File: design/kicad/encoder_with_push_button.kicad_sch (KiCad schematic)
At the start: 1 part

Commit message: Refactor code structure for improved readability and maintainability
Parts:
- added D4, D5, D6: PESD5V0L1BA,115, KiCad:SOD2512X110N, symbol PESD5V0L1BA_115:PESD5V0L1BA,115
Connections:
- net QUAD_A: now also D4.1 (K1)
- net QUAD_B: now also D5.1 (K1)
- net SW_A: now also D6.1 (K1)
- new net GND: D4.2 (K2), D5.2 (K2), D6.2 (K2)

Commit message: Add schematic for MIDI Display MSP2807 with associated components
- Created a new schematic file for the MIDI Display MSP2807.
- Included a unpolarized capacitor (C2) with a value of 100nF.
- Added properties such as reference, value, footprint, and datasheet for the capacitor.
- Integrated the MIDI Display module with detailed pin configurations and properties.
- Defined hierarchical labels for power and data connections (VCC, GND, CS, RST, DC, etc.).
- Ensured all components are marked for BOM inclusion and simulation.
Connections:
- net QUAD_GND is gone; now on net GND: ENC_MECH1.C (GND)
- net SW_GND is gone; now on net GND: ENC_MECH1.2 (GND)
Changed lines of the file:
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@@
-	(wire
-		(pts
-			(xy 50.8 76.2) (xy 87.63 76.2)
-		)
-		(stroke
-			(width 0)
-			(type default)
-		)
-	)
-	(wire
-		(pts
-			(xy 115.57 78.74) (xy 118.11 78.74)
-		)
-		(stroke
-			(width 0)
-			(type default)
-		)
-	)
 	(wire
 		(pts
@@
 	(wire
 		(pts
+			(xy 115.57 78.74) (xy 116.84 78.74)
+		)
+		(stroke
+			(width 0)
+			(type default)
+		)
+	)
+	(wire
+		(pts
 			(xy 50.8 91.44) (xy 63.5 91.44)
 		)
@@
 	(wire
 		(pts
+			(xy 86.36 76.2) (xy 87.63 76.2)
+		)
+		(stroke
+			(width 0)
+			(type default)
+		)
+	)
+	(wire
+		(pts
 			(xy 86.36 78.74) (xy 87.63 78.74)
 		)
@@
 			(width 0)
 			(type default)
+		)
+	)
+	(global_label "GND"
+		(shape input)
+		(at 116.84 78.74 0)
+		(fields_autoplaced yes)
+		(effects
+			(font
+				(size 1.27 1.27)
+			)
+			(justify left)
+		)
+		(property "Intersheetrefs" "${INTERSHEET_REFS}"
+			(at 123.6957 78.74 0)
+			(effects
+				(font
+					(size 1.27 1.27)
+				)
+				(justify left)
+				(hide yes)
+			)
+		)
+	)
+	(global_label "GND"
+		(shape input)
+		(at 86.36 76.2 180)
+		(fields_autoplaced yes)
+		(effects
+			(font
+				(size 1.27 1.27)
+			)
+			(justify right)
+		)
+		(property "Intersheetrefs" "${INTERSHEET_REFS}"
+			(at 79.5043 76.2 0)
+			(effects
+				(font
+					(size 1.27 1.27)
+				)
+				(justify right)
+				(hide yes)
+			)
 		)
 	)
@@
 		)
 	)
-	(hierarchical_label "QUAD_GND"
-		(shape passive)
-		(at 50.8 76.2 180)
-		(effects
-			(font
-				(size 1.27 1.27)
-			)
-			(justify right)
-		)
-	)
-	(hierarchical_label "SW_GND"
-		(shape passive)
-		(at 118.11 78.74 0)
-		(effects
-			(font
-				(size 1.27 1.27)
-			)
-			(justify left)
-		)
-	)

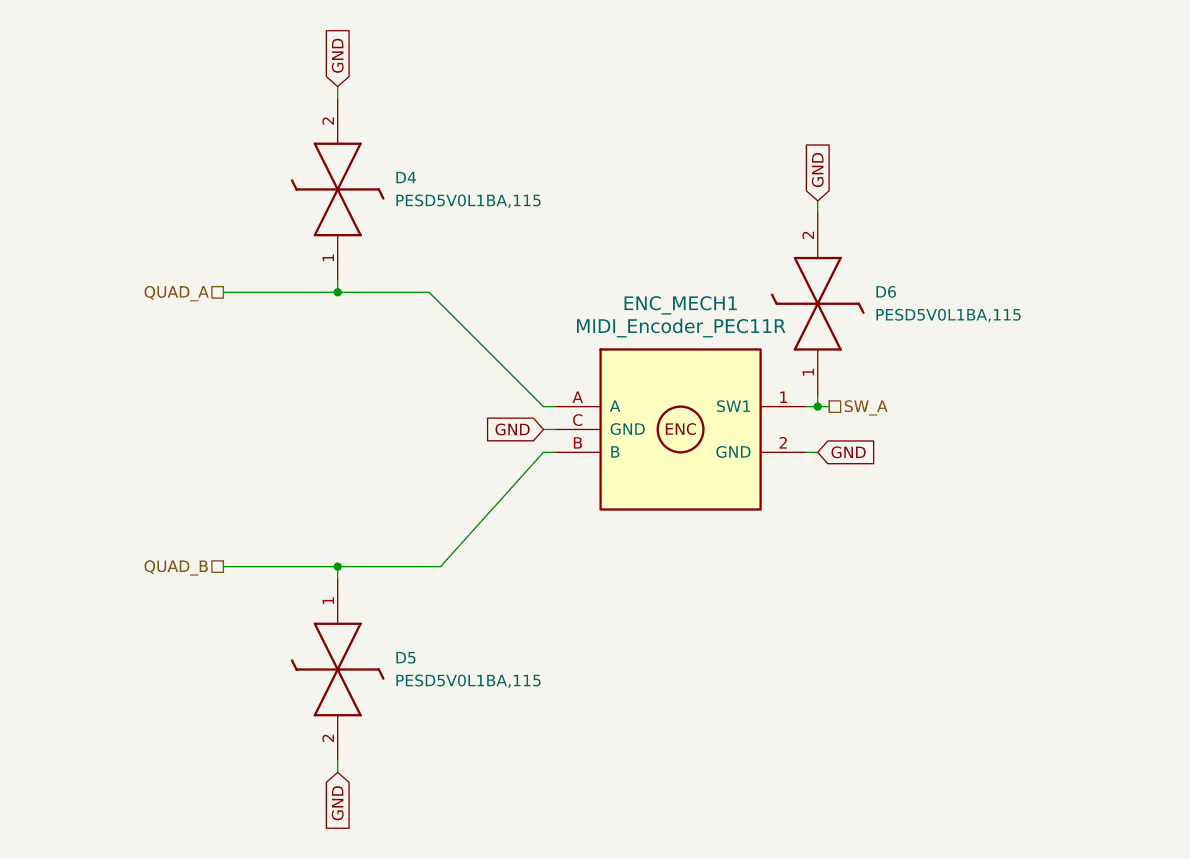
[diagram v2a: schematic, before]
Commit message: Fix net format name and update junctions in MIDI controller schematic
- Set net format name to "KiCad" in the project file.
- Added multiple junctions at specified coordinates in the schematic.
- Adjusted existing junction positions and UUIDs for consistency.
- Updated wire connections to reflect new junction placements.
- Corrected component references and properties for various components.
- Added new capacitor symbols with appropriate properties and references.
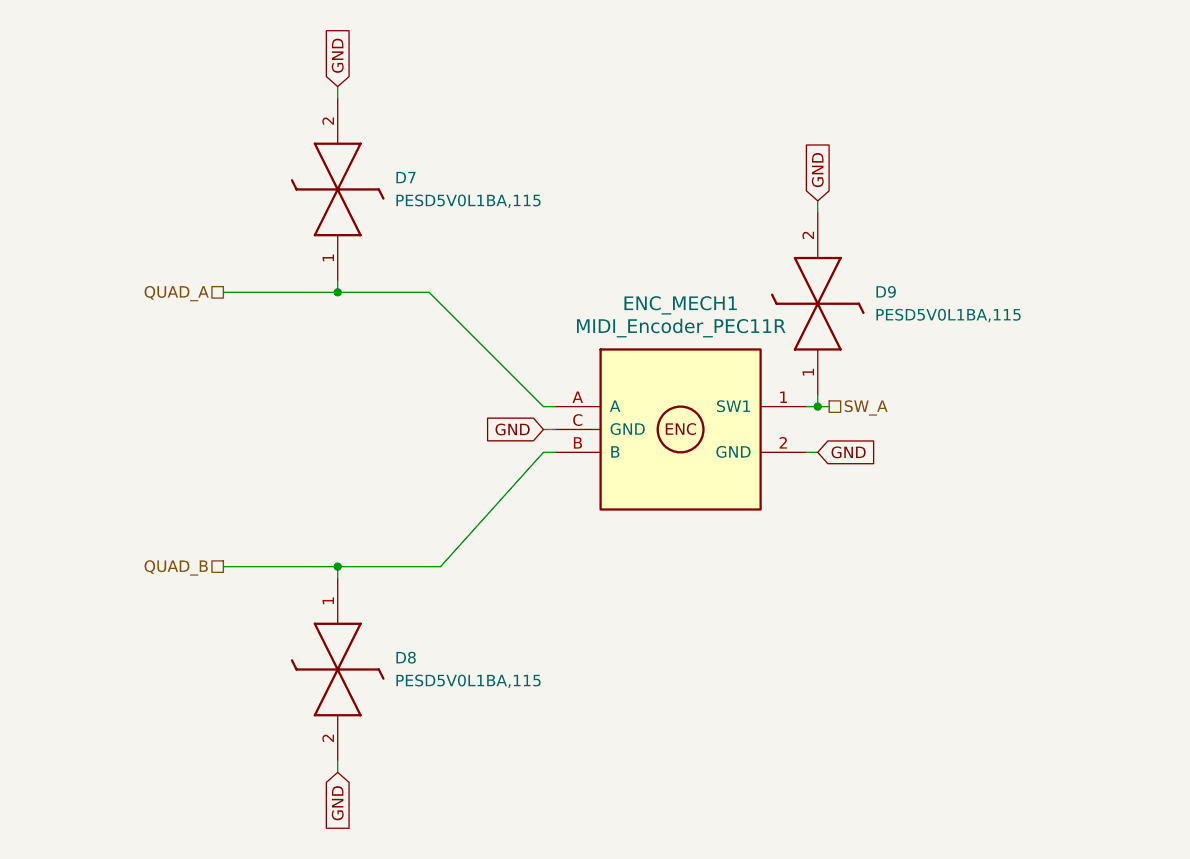
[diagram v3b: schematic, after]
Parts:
- renumbered D4 to D7, D5 to D8, D6 to D9
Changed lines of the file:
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@@
 		(dnp no)
 		(fields_autoplaced yes)
-		(property "Reference" "D4"
+		(property "Reference" "D7"
 			(at 69.85 48.2599 90)
 			(effects
@@
 			(project "midi_controller"
 				(path "/9e44e663-00d0-4f33-bf1f-c4ad78deb554/f2987add-55a5-4c89-9b33-db7ed86a6cdc"
+					(reference "D31")
+					(unit 1)
+				)
+				(path "/9e44e663-00d0-4f33-bf1f-c4ad78deb554/8b3bc88b-b526-44d8-9760-500b43fd5a71/0ace1318-b253-4d85-b784-aa61ad0f89cd"
+					(reference "D10")
+					(unit 1)
+				)
+				(path "/9e44e663-00d0-4f33-bf1f-c4ad78deb554/8b3bc88b-b526-44d8-9760-500b43fd5a71/1413c73c-0ad0-4a10-833c-ff3e4825f086"
+					(reference "D22")
+					(unit 1)
+				)
+				(path "/9e44e663-00d0-4f33-bf1f-c4ad78deb554/8b3bc88b-b526-44d8-9760-500b43fd5a71/24f763b3-d9d2-44ca-b0de-e5bd6d783cf4"
+					(reference "D25")
+					(unit 1)
+				)
+				(path "/9e44e663-00d0-4f33-bf1f-c4ad78deb554/8b3bc88b-b526-44d8-9760-500b43fd5a71/291f4e39-6718-4dda-83a6-20f8f943b75d"
+					(reference "D13")
+					(unit 1)
+				)
+				(path "/9e44e663-00d0-4f33-bf1f-c4ad78deb554/8b3bc88b-b526-44d8-9760-500b43fd5a71/3c9339b8-42f1-40cb-9183-aa88346af463"
+					(reference "D16")
+					(unit 1)
+				)
+				(path "/9e44e663-00d0-4f33-bf1f-c4ad78deb554/8b3bc88b-b526-44d8-9760-500b43fd5a71/4af660a9-1b0e-40bf-ba48-b976c7e464d4"
+					(reference "D19")
+					(unit 1)
+				)
+				(path "/9e44e663-00d0-4f33-bf1f-c4ad78deb554/8b3bc88b-b526-44d8-9760-500b43fd5a71/60e25267-b738-456c-86e0-26223ee5fe23"
+					(reference "D7")
+					(unit 1)
+				)
+				(path "/9e44e663-00d0-4f33-bf1f-c4ad78deb554/8b3bc88b-b526-44d8-9760-500b43fd5a71/761c51eb-8364-4d00-98cb-27a8734a6aa5"
 					(reference "D28")
-					(unit 1)
-				)
-				(path "/9e44e663-00d0-4f33-bf1f-c4ad78deb554/8b3bc88b-b526-44d8-9760-500b43fd5a71/0ace1318-b253-4d85-b784-aa61ad0f89cd"
-					(reference "D7")
-					(unit 1)
-				)
-				(path "/9e44e663-00d0-4f33-bf1f-c4ad78deb554/8b3bc88b-b526-44d8-9760-500b43fd5a71/1413c73c-0ad0-4a10-833c-ff3e4825f086"
-					(reference "D19")
-					(unit 1)
-				)
-				(path "/9e44e663-00d0-4f33-bf1f-c4ad78deb554/8b3bc88b-b526-44d8-9760-500b43fd5a71/24f763b3-d9d2-44ca-b0de-e5bd6d783cf4"
-					(reference "D22")
-					(unit 1)
-				)
-				(path "/9e44e663-00d0-4f33-bf1f-c4ad78deb554/8b3bc88b-b526-44d8-9760-500b43fd5a71/291f4e39-6718-4dda-83a6-20f8f943b75d"
-					(reference "D10")
-					(unit 1)
-				)
-				(path "/9e44e663-00d0-4f33-bf1f-c4ad78deb554/8b3bc88b-b526-44d8-9760-500b43fd5a71/3c9339b8-42f1-40cb-9183-aa88346af463"
-					(reference "D13")
-					(unit 1)
-				)
-				(path "/9e44e663-00d0-4f33-bf1f-c4ad78deb554/8b3bc88b-b526-44d8-9760-500b43fd5a71/4af660a9-1b0e-40bf-ba48-b976c7e464d4"
-					(reference "D16")
-					(unit 1)
-				)
-				(path "/9e44e663-00d0-4f33-bf1f-c4ad78deb554/8b3bc88b-b526-44d8-9760-500b43fd5a71/60e25267-b738-456c-86e0-26223ee5fe23"
-					(reference "D4")
-					(unit 1)
-				)
-				(path "/9e44e663-00d0-4f33-bf1f-c4ad78deb554/8b3bc88b-b526-44d8-9760-500b43fd5a71/761c51eb-8364-4d00-98cb-27a8734a6aa5"
-					(reference "D25")
 					(unit 1)
 				)
@@
 		(dnp no)
 		(fields_autoplaced yes)
-		(property "Reference" "D5"
+		(property "Reference" "D8"
 			(at 69.85 101.5999 90)
 			(effects
@@
 			(project "midi_controller"
 				(path "/9e44e663-00d0-4f33-bf1f-c4ad78deb554/f2987add-55a5-4c89-9b33-db7ed86a6cdc"
+					(reference "D32")
+					(unit 1)
+				)
+				(path "/9e44e663-00d0-4f33-bf1f-c4ad78deb554/8b3bc88b-b526-44d8-9760-500b43fd5a71/0ace1318-b253-4d85-b784-aa61ad0f89cd"
+					(reference "D11")
+					(unit 1)
+				)
+				(path "/9e44e663-00d0-4f33-bf1f-c4ad78deb554/8b3bc88b-b526-44d8-9760-500b43fd5a71/1413c73c-0ad0-4a10-833c-ff3e4825f086"
+					(reference "D23")
+					(unit 1)
+				)
+				(path "/9e44e663-00d0-4f33-bf1f-c4ad78deb554/8b3bc88b-b526-44d8-9760-500b43fd5a71/24f763b3-d9d2-44ca-b0de-e5bd6d783cf4"
+					(reference "D26")
+					(unit 1)
+				)
+				(path "/9e44e663-00d0-4f33-bf1f-c4ad78deb554/8b3bc88b-b526-44d8-9760-500b43fd5a71/291f4e39-6718-4dda-83a6-20f8f943b75d"
+					(reference "D14")
+					(unit 1)
+				)
+				(path "/9e44e663-00d0-4f33-bf1f-c4ad78deb554/8b3bc88b-b526-44d8-9760-500b43fd5a71/3c9339b8-42f1-40cb-9183-aa88346af463"
+					(reference "D17")
+					(unit 1)
+				)
+				(path "/9e44e663-00d0-4f33-bf1f-c4ad78deb554/8b3bc88b-b526-44d8-9760-500b43fd5a71/4af660a9-1b0e-40bf-ba48-b976c7e464d4"
+					(reference "D20")
+					(unit 1)
+				)
+				(path "/9e44e663-00d0-4f33-bf1f-c4ad78deb554/8b3bc88b-b526-44d8-9760-500b43fd5a71/60e25267-b738-456c-86e0-26223ee5fe23"
+					(reference "D8")
+					(unit 1)
+				)
+				(path "/9e44e663-00d0-4f33-bf1f-c4ad78deb554/8b3bc88b-b526-44d8-9760-500b43fd5a71/761c51eb-8364-4d00-98cb-27a8734a6aa5"
 					(reference "D29")
-					(unit 1)
-				)
-				(path "/9e44e663-00d0-4f33-bf1f-c4ad78deb554/8b3bc88b-b526-44d8-9760-500b43fd5a71/0ace1318-b253-4d85-b784-aa61ad0f89cd"
-					(reference "D8")
-					(unit 1)
-				)
-				(path "/9e44e663-00d0-4f33-bf1f-c4ad78deb554/8b3bc88b-b526-44d8-9760-500b43fd5a71/1413c73c-0ad0-4a10-833c-ff3e4825f086"
-					(reference "D20")
-					(unit 1)
-				)
-				(path "/9e44e663-00d0-4f33-bf1f-c4ad78deb554/8b3bc88b-b526-44d8-9760-500b43fd5a71/24f763b3-d9d2-44ca-b0de-e5bd6d783cf4"
-					(reference "D23")
-					(unit 1)
-				)
-				(path "/9e44e663-00d0-4f33-bf1f-c4ad78deb554/8b3bc88b-b526-44d8-9760-500b43fd5a71/291f4e39-6718-4dda-83a6-20f8f943b75d"
-					(reference "D11")
-					(unit 1)
-				)
-				(path "/9e44e663-00d0-4f33-bf1f-c4ad78deb554/8b3bc88b-b526-44d8-9760-500b43fd5a71/3c9339b8-42f1-40cb-9183-aa88346af463"
-					(reference "D14")
-					(unit 1)
-				)
-				(path "/9e44e663-00d0-4f33-bf1f-c4ad78deb554/8b3bc88b-b526-44d8-9760-500b43fd5a71/4af660a9-1b0e-40bf-ba48-b976c7e464d4"
-					(reference "D17")
-					(unit 1)
-				)
-				(path "/9e44e663-00d0-4f33-bf1f-c4ad78deb554/8b3bc88b-b526-44d8-9760-500b43fd5a71/60e25267-b738-456c-86e0-26223ee5fe23"
-					(reference "D5")
-					(unit 1)
-				)
-				(path "/9e44e663-00d0-4f33-bf1f-c4ad78deb554/8b3bc88b-b526-44d8-9760-500b43fd5a71/761c51eb-8364-4d00-98cb-27a8734a6aa5"
-					(reference "D26")
 					(unit 1)
 				)
@@
 		(dnp no)
 		(fields_autoplaced yes)
-		(property "Reference" "D6"
+		(property "Reference" "D9"
 			(at 123.19 60.9599 90)
 			(effects
@@
 			(project "midi_controller"
 				(path "/9e44e663-00d0-4f33-bf1f-c4ad78deb554/f2987add-55a5-4c89-9b33-db7ed86a6cdc"
+					(reference "D33")
+					(unit 1)
+				)
+				(path "/9e44e663-00d0-4f33-bf1f-c4ad78deb554/8b3bc88b-b526-44d8-9760-500b43fd5a71/0ace1318-b253-4d85-b784-aa61ad0f89cd"
+					(reference "D12")
+					(unit 1)
+				)
+				(path "/9e44e663-00d0-4f33-bf1f-c4ad78deb554/8b3bc88b-b526-44d8-9760-500b43fd5a71/1413c73c-0ad0-4a10-833c-ff3e4825f086"
+					(reference "D24")
+					(unit 1)
+				)
+				(path "/9e44e663-00d0-4f33-bf1f-c4ad78deb554/8b3bc88b-b526-44d8-9760-500b43fd5a71/24f763b3-d9d2-44ca-b0de-e5bd6d783cf4"
+					(reference "D27")
+					(unit 1)
+				)
+				(path "/9e44e663-00d0-4f33-bf1f-c4ad78deb554/8b3bc88b-b526-44d8-9760-500b43fd5a71/291f4e39-6718-4dda-83a6-20f8f943b75d"
+					(reference "D15")
+					(unit 1)
+				)
+				(path "/9e44e663-00d0-4f33-bf1f-c4ad78deb554/8b3bc88b-b526-44d8-9760-500b43fd5a71/3c9339b8-42f1-40cb-9183-aa88346af463"
+					(reference "D18")
+					(unit 1)
+				)
+				(path "/9e44e663-00d0-4f33-bf1f-c4ad78deb554/8b3bc88b-b526-44d8-9760-500b43fd5a71/4af660a9-1b0e-40bf-ba48-b976c7e464d4"
+					(reference "D21")
+					(unit 1)
+				)
+				(path "/9e44e663-00d0-4f33-bf1f-c4ad78deb554/8b3bc88b-b526-44d8-9760-500b43fd5a71/60e25267-b738-456c-86e0-26223ee5fe23"
+					(reference "D9")
+					(unit 1)
+				)
+				(path "/9e44e663-00d0-4f33-bf1f-c4ad78deb554/8b3bc88b-b526-44d8-9760-500b43fd5a71/761c51eb-8364-4d00-98cb-27a8734a6aa5"
 					(reference "D30")
 					(unit 1)
 				)
-				(path "/9e44e663-00d0-4f33-bf1f-c4ad78deb554/8b3bc88b-b526-44d8-9760-500b43fd5a71/0ace1318-b253-4d85-b784-aa61ad0f89cd"
-					(reference "D9")
-					(unit 1)
-				)
-				(path "/9e44e663-00d0-4f33-bf1f-c4ad78deb554/8b3bc88b-b526-44d8-9760-500b43fd5a71/1413c73c-0ad0-4a10-833c-ff3e4825f086"
-					(reference "D21")
-					(unit 1)
-				)
-				(path "/9e44e663-00d0-4f33-bf1f-c4ad78deb554/8b3bc88b-b526-44d8-9760-500b43fd5a71/24f763b3-d9d2-44ca-b0de-e5bd6d783cf4"
-					(reference "D24")
-					(unit 1)
-				)
-				(path "/9e44e663-00d0-4f33-bf1f-c4ad78deb554/8b3bc88b-b526-44d8-9760-500b43fd5a71/291f4e39-6718-4dda-83a6-20f8f943b75d"
-					(reference "D12")
-					(unit 1)
-				)
-				(path "/9e44e663-00d0-4f33-bf1f-c4ad78deb554/8b3bc88b-b526-44d8-9760-500b43fd5a71/3c9339b8-42f1-40cb-9183-aa88346af463"
-					(reference "D15")
-					(unit 1)
-				)
-				(path "/9e44e663-00d0-4f33-bf1f-c4ad78deb554/8b3bc88b-b526-44d8-9760-500b43fd5a71/4af660a9-1b0e-40bf-ba48-b976c7e464d4"
-					(reference "D18")
-					(unit 1)
-				)
-				(path "/9e44e663-00d0-4f33-bf1f-c4ad78deb554/8b3bc88b-b526-44d8-9760-500b43fd5a71/60e25267-b738-456c-86e0-26223ee5fe23"
-					(reference "D6")
-					(unit 1)
-				)
-				(path "/9e44e663-00d0-4f33-bf1f-c4ad78deb554/8b3bc88b-b526-44d8-9760-500b43fd5a71/761c51eb-8364-4d00-98cb-27a8734a6aa5"
-					(reference "D27")
-					(unit 1)
-				)
